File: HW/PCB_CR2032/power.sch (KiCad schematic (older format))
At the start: 6 parts

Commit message: * Updated Schematic with 1206 leds and 1k 0805 current limiting resistors
* Restored STDC14 and debug UART, now shared with top led of minute and second. Some other LED pins remapped

* Updated STM32CubeMX project to reflect schematic changes and generated code again
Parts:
- C11: Make Murata -> Yageo; Mouser 81-GRM21BR71A106KA73K -> 603-CC805KKX7R6BB106; Part GRM21BR71A106KA73K -> CC0805KKX7R6BB106
- D1, D2: Make (none) -> ST; Mouser (none) -> 511-BAR43CFILM; Part (none) -> BAR43CFILM
- R27: Make (none) -> Yageo; Mouser (none) -> 603-RC0805FR-0710KL; Part (none) -> RC0805FR-0710KL
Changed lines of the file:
@@
 F 2 "Package_TO_SOT_SMD:SOT-23_Handsoldering" H 6000 3350 50  0001 C CNN
 F 3 "~" H 6000 3350 50  0001 C CNN
+F 4 "ST" H 6000 3350 50  0001 C CNN "Make"
+F 5 "511-BAR43CFILM" H 6000 3350 50  0001 C CNN "Mouser"
+F 6 "BAR43CFILM" H 6000 3350 50  0001 C CNN "Part"
 	1    6000 3350
 	1    0    0    -1
@@
 F 2 "Capacitor_SMD:C_0805_2012Metric_Pad1.15x1.40mm_HandSolder" H 7238 3350 50  0001 C CNN
 F 3 "~" H 7200 3500 50  0001 C CNN
-F 4 "Murata" H 7200 3500 50  0001 C CNN "Make"
-F 5 "GRM21BR71A106KA73K" H 7200 3500 50  0001 C CNN "Part"
-F 6 "81-GRM21BR71A106KA73K" H 7200 3500 50  0001 C CNN "Mouser"
+F 4 "Yageo" H 7200 3500 50  0001 C CNN "Make"
+F 5 "CC0805KKX7R6BB106" H 7200 3500 50  0001 C CNN "Part"
+F 6 "603-CC805KKX7R6BB106" H 7200 3500 50  0001 C CNN "Mouser"
 	1    7200 3500
 	1    0    0    -1
@@
 F 2 "Resistor_SMD:R_0805_2012Metric_Pad1.15x1.40mm_HandSolder" V 5380 3350 50  0001 C CNN
 F 3 "~" H 5450 3350 50  0001 C CNN
+F 4 "Yageo" H 5450 3350 50  0001 C CNN "Make"
+F 5 "603-RC0805FR-0710KL" H 5450 3350 50  0001 C CNN "Mouser"
+F 6 "RC0805FR-0710KL" H 5450 3350 50  0001 C CNN "Part"
 	1    5450 3350
 	0    1    1    0
@@
 F 2 "Package_TO_SOT_SMD:SOT-23_Handsoldering" H 6900 3250 50  0001 C CNN
 F 3 "~" H 6900 3250 50  0001 C CNN
+F 4 "ST" H 6900 3250 50  0001 C CNN "Make"
+F 5 "511-BAR43CFILM" H 6900 3250 50  0001 C CNN "Mouser"
+F 6 "BAR43CFILM" H 6900 3250 50  0001 C CNN "Part"
 	1    6900 3250
 	0    -1   -1   0

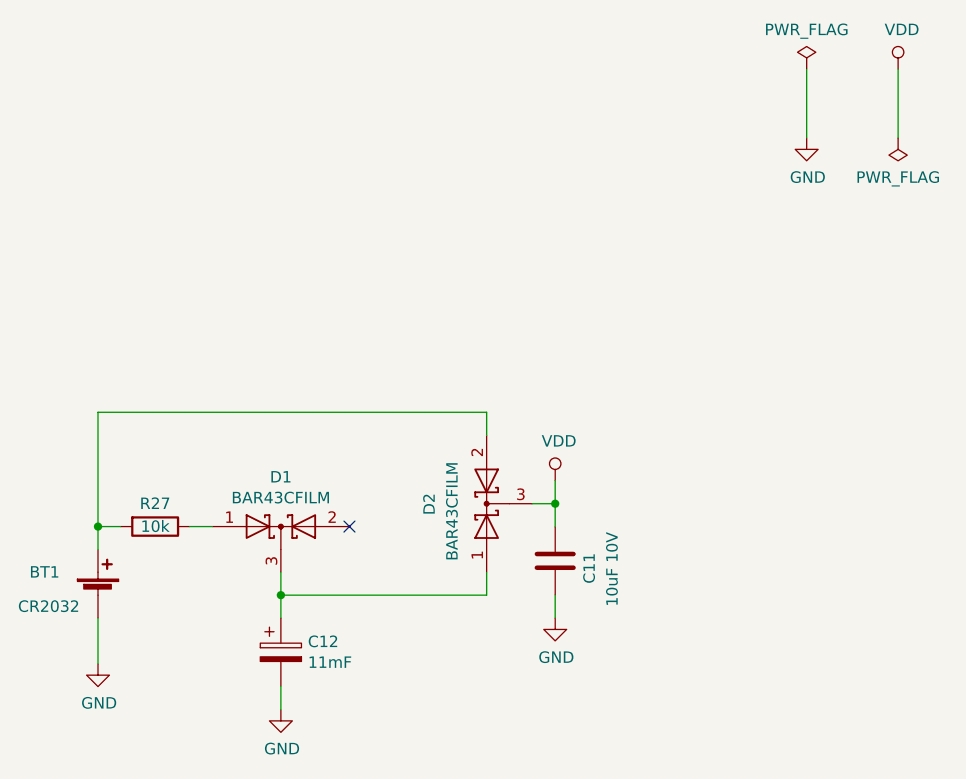
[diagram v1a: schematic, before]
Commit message: Created layout for CR2032 version 1.0, for first prototype order, resulted in a lot of changes in the pin-mapping to make routing easier.
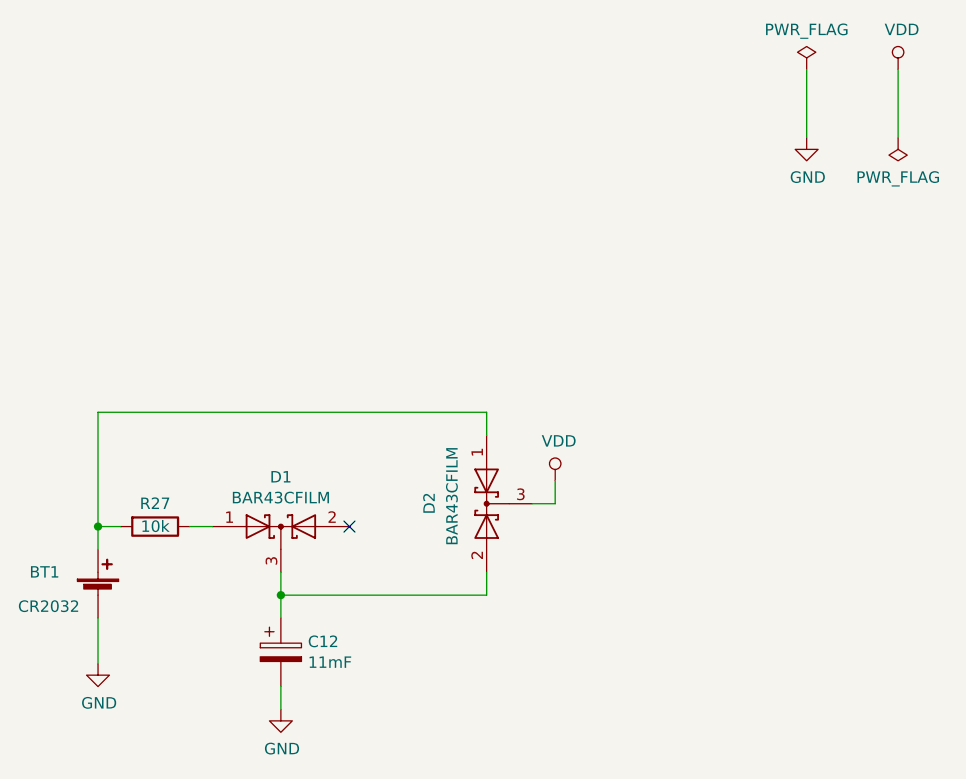
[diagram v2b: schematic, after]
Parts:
- removed C11: 10uF 10V, Capacitor_SMD:C_0805_2012Metric_Pad1.15x1.40mm_HandSolder, symbol Device:C
- R27: footprint Resistor_SMD:R_0805_2012Metric_Pad1.15x1.40mm_HandSolder -> Resistor_SMD:R_0603_1608Metric_Pad1.05x0.95mm_HandSolder; LCSC (none) -> C25804; Make Yageo -> (none); Mouser 603-RC0805FR-0710KL -> (none); Part RC0805FR-0710KL -> (none); jlcpcb (none) -> 0603WAF1002T5E
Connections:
- net at BT1.1 (+), R27.2: now also D2.1 (A); no longer D2.2 (A)
- net at C12.1, D1.3 (K): now also D2.2 (A); no longer D2.1 (A)
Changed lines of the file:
@@
-	1    0    0    -1
-$EndComp
-$Comp
-L Device:C C?
-U 1 1 5DC4CF0A
-P 7200 3500
-AR Path="/5DC1DE5A/5DC4CF0A" Ref="C?"  Part="1"
-AR Path="/5DC4CF0A" Ref="C?"  Part="1"
-AR Path="/5DC4948F/5DC4CF0A" Ref="C11"  Part="1"
-F 0 "C11" V 7350 3400 50  0000 L CNN
-F 1 "10uF 10V" V 7450 3300 50  0000 L CNN
-F 2 "Capacitor_SMD:C_0805_2012Metric_Pad1.15x1.40mm_HandSolder" H 7238 3350 50  0001 C CNN
-F 3 "~" H 7200 3500 50  0001 C CNN
-F 4 "Yageo" H 7200 3500 50  0001 C CNN "Make"
-F 5 "CC0805KKX7R6BB106" H 7200 3500 50  0001 C CNN "Part"
-F 6 "603-CC805KKX7R6BB106" H 7200 3500 50  0001 C CNN "Mouser"
-	1    7200 3500
 	1    0    0    -1
 $EndComp
@@
 F 0 "R27" V 5350 3350 50  0000 C CNN
 F 1 "10k" V 5450 3350 50  0000 C CNN
-F 2 "Resistor_SMD:R_0805_2012Metric_Pad1.15x1.40mm_HandSolder" V 5380 3350 50  0001 C CNN
+F 2 "Resistor_SMD:R_0603_1608Metric_Pad1.05x0.95mm_HandSolder" V 5380 3350 50  0001 C CNN
 F 3 "~" H 5450 3350 50  0001 C CNN
-F 4 "Yageo" H 5450 3350 50  0001 C CNN "Make"
-F 5 "603-RC0805FR-0710KL" H 5450 3350 50  0001 C CNN "Mouser"
-F 6 "RC0805FR-0710KL" H 5450 3350 50  0001 C CNN "Part"
+F 4 "" H 5450 3350 50  0001 C CNN "Make"
+F 5 "" H 5450 3350 50  0001 C CNN "Mouser"
+F 6 "" H 5450 3350 50  0001 C CNN "Part"
+F 7 "C25804" H 5450 3350 50  0001 C CNN "LCSC"
+F 8 "0603WAF1002T5E" H 5450 3350 50  0001 C CNN "jlcpcb"
 	1    5450 3350
 	0    1    1    0
@@
 F 6 "BAR43CFILM" H 6900 3250 50  0001 C CNN "Part"
 	1    6900 3250
-	0    -1   -1   0
+	0    -1   1    0
 $EndComp
 $Comp
@@
 	1    0    0    -1
 $EndComp
-$Comp
-L power:GND #PWR?
-U 1 1 5DCA0DFD
-P 7200 3750
-AR Path="/5DCA0DFD" Ref="#PWR?"  Part="1"
-AR Path="/5DC4948F/5DCA0DFD" Ref="#PWR034"  Part="1"
-F 0 "#PWR034" H 7200 3500 50  0001 C CNN
-F 1 "GND" H 7205 3577 50  0000 C CNN
-F 2 "" H 7200 3750 50  0001 C CNN
-F 3 "" H 7200 3750 50  0001 C CNN
-	1    7200 3750
-	1    0    0    -1
-$EndComp
 Wire Wire Line
 	7100 3250 7200 3250
@@
 	7200 3250 7200 3150
 Wire Wire Line
-	7200 3750 7200 3650
-Wire Wire Line
-	7200 3350 7200 3250
-Connection ~ 7200 3250
-Wire Wire Line
 	6000 4150 6000 4050

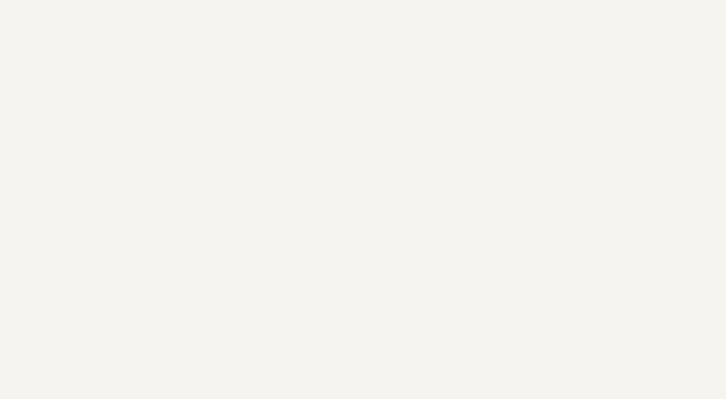
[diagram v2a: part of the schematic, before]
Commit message: Worked on Rev 2.0 HW with smaller size.
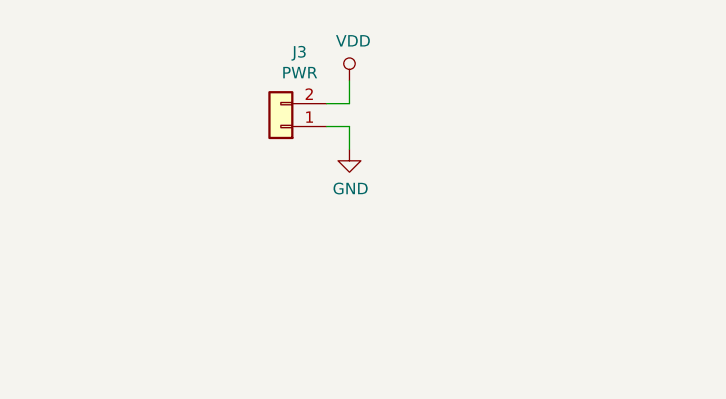
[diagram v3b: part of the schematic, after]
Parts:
- added J3: PWR, Connector_PinHeader_1.27mm:PinHeader_1x02_P1.27mm_Vertical, symbol Connector_Generic:Conn_01x02
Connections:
- net GND: now also J3.1 (Pin_1)
- net VDD: now also J3.2 (Pin_2)
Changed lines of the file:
@@
 Wire Wire Line
 	8300 1650 8300 1350
+$Comp
+L Connector_Generic:Conn_01x02 J3
+U 1 1 5DCE1F2A
+P 6000 1600
+F 0 "J3" H 5918 1275 50  0000 C CNN
+F 1 "PWR" H 5918 1366 50  0000 C CNN
+F 2 "Connector_PinHeader_1.27mm:PinHeader_1x02_P1.27mm_Vertical" H 6000 1600 50  0001 C CNN
+F 3 "~" H 6000 1600 50  0001 C CNN
+	1    6000 1600
+	-1   0    0    1
+$EndComp
+$Comp
+L power:GND #PWR?
+U 1 1 5DCE2A7F
+P 6300 1700
+AR Path="/5DCE2A7F" Ref="#PWR?"  Part="1"
+AR Path="/5DC4948F/5DCE2A7F" Ref="#PWR0102"  Part="1"
+F 0 "#PWR0102" H 6300 1450 50  0001 C CNN
+F 1 "GND" H 6305 1527 50  0000 C CNN
+F 2 "" H 6300 1700 50  0001 C CNN
+F 3 "" H 6300 1700 50  0001 C CNN
+	1    6300 1700
+	1    0    0    -1
+$EndComp
+$Comp
+L power:VDD #PWR?
+U 1 1 5DCE3453
+P 6300 1400
+AR Path="/5DCE3453" Ref="#PWR?"  Part="1"
+AR Path="/5DC4948F/5DCE3453" Ref="#PWR0103"  Part="1"
+F 0 "#PWR0103" H 6300 1250 50  0001 C CNN
+F 1 "VDD" H 6317 1573 50  0000 C CNN
+F 2 "" H 6300 1400 50  0001 C CNN
+F 3 "" H 6300 1400 50  0001 C CNN
+	1    6300 1400
+	1    0    0    -1
+$EndComp
+Wire Wire Line
+	6200 1500 6300 1500
+Wire Wire Line
+	6300 1500 6300 1400
+Wire Wire Line
+	6200 1600 6300 1600
+Wire Wire Line
+	6300 1600 6300 1700
 $EndSCHEMATC
